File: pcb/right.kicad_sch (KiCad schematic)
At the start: 114 parts, among them J1 PJ-320A, SW1 -, SW10 O, SW11 I, SW12 U, SW13 Y, SW14 ', SW15 ;, SW16 L, SW17 K, SW18 J, SW19 H, SW2 0, SW20 Alt, SW21 Shift, SW22 /, SW23 ., SW24 ,, SW25 M, SW26 N, SW27 Ctrl, SW28 ], SW29 [, SW3 9, SW30 Down, SW31 Up, SW32 Fn, SW33 Space, SW34 Enter, SW4 8, SW5 7, SW6 6, SW8 \, SW9 P, SW90 MSK12C02 power, SW91 Reset, U1 nRF52840 Pro Micro

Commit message: Merge both halves into one KiCad project
pcb/keygen.kicad_pro holds a top sheet with left and right sub-sheets
(refs 1xx/2xx, sheet-local nets) and will carry one PCB with both halves
joined by snap-off tabs. The board stays non-reversible. The checker now
runs ERC on the whole project and splits the netlist per half.
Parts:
- removed BT1: LiPo 3.7V ~1000mAh, Connector_JST:JST_PH_S2B-PH-K_1x02_P2.00mm_Horizontal, symbol Device:Battery_Cell
- removed C1: 10uF, Capacitor_SMD:C_0805_2012Metric, symbol Device:C
- removed C2: 100nF, Capacitor_SMD:C_0805_2012Metric, symbol Device:C
- removed D1, D10, D11, D12, D13, D14, D15, D16, D17, D18, D19, D2, D20, D21, D22, D23, D24, D25, D26, D27, D28, D29, D3, D30, D31, D32, D33, D34, D4, D5, D6, D7, D8, D9: 1N4148, Diode_THT:D_DO-35_SOD27_P7.62mm_Horizontal, symbol Device:D
- removed ENC1: EC11, Rotary_Encoder:RotaryEncoder_Alps_EC11E-Switch_Vertical_H20mm, symbol Device:RotaryEncoder_Switch
- removed J1: PJ-320A, Keebio-Parts:TRRS-PJ-320A, symbol keygen:TRRS_PJ-320A
- removed LED1, LED10, LED11, LED12, LED13, LED14, LED15, LED16, LED17, LED18, LED19, LED2, LED20, LED21, LED22, LED23, LED24, LED25, LED26, LED27, LED28, LED29, LED3, LED30, LED31, LED32, LED33, LED34, LED35, LED36, LED37, LED38, LED39, LED4, LED5, LED6, LED7, LED8, LED9: SK6812MINI-E, LED_SMD:LED_SK6812MINI-E_3.2x2.8mm_P1.5mm_ReverseMount, symbol LED:SK6812MINI-E
- removed SW1: -, marbastlib-mx:SW_MX_HS_CPG151101S11_1.25u, symbol marbastlib-mx:MX_SW_HS_CPG151101S11
- removed SW10: O, marbastlib-mx:SW_MX_HS_CPG151101S11_1u, symbol marbastlib-mx:MX_SW_HS_CPG151101S11
- removed SW11: I, marbastlib-mx:SW_MX_HS_CPG151101S11_1u, symbol marbastlib-mx:MX_SW_HS_CPG151101S11
- removed SW12: U, marbastlib-mx:SW_MX_HS_CPG151101S11_1u, symbol marbastlib-mx:MX_SW_HS_CPG151101S11
- removed SW13: Y, marbastlib-mx:SW_MX_HS_CPG151101S11_1u, symbol marbastlib-mx:MX_SW_HS_CPG151101S11
- removed SW14: ', marbastlib-mx:SW_MX_HS_CPG151101S11_1.25u, symbol marbastlib-mx:MX_SW_HS_CPG151101S11
- removed SW15: ;, marbastlib-mx:SW_MX_HS_CPG151101S11_1u, symbol marbastlib-mx:MX_SW_HS_CPG151101S11
- removed SW16: L, marbastlib-mx:SW_MX_HS_CPG151101S11_1u, symbol marbastlib-mx:MX_SW_HS_CPG151101S11
- removed SW17: K, marbastlib-mx:SW_MX_HS_CPG151101S11_1u, symbol marbastlib-mx:MX_SW_HS_CPG151101S11
- removed SW18: J, marbastlib-mx:SW_MX_HS_CPG151101S11_1u, symbol marbastlib-mx:MX_SW_HS_CPG151101S11
- removed SW19: H, marbastlib-mx:SW_MX_HS_CPG151101S11_1u, symbol marbastlib-mx:MX_SW_HS_CPG151101S11
- removed SW2: 0, marbastlib-mx:SW_MX_HS_CPG151101S11_1u, symbol marbastlib-mx:MX_SW_HS_CPG151101S11
- removed SW20: Alt, marbastlib-mx:SW_MX_HS_CPG151101S11_1u, symbol marbastlib-mx:MX_SW_HS_CPG151101S11
- removed SW21: Shift, marbastlib-mx:SW_MX_HS_CPG151101S11_1.25u, symbol marbastlib-mx:MX_SW_HS_CPG151101S11
- removed SW22: /, marbastlib-mx:SW_MX_HS_CPG151101S11_1u, symbol marbastlib-mx:MX_SW_HS_CPG151101S11
- removed SW23: ., marbastlib-mx:SW_MX_HS_CPG151101S11_1u, symbol marbastlib-mx:MX_SW_HS_CPG151101S11
- removed SW24: ,, marbastlib-mx:SW_MX_HS_CPG151101S11_1u, symbol marbastlib-mx:MX_SW_HS_CPG151101S11
- removed SW25: M, marbastlib-mx:SW_MX_HS_CPG151101S11_1u, symbol marbastlib-mx:MX_SW_HS_CPG151101S11
- removed SW26: N, marbastlib-mx:SW_MX_HS_CPG151101S11_1u, symbol marbastlib-mx:MX_SW_HS_CPG151101S11
- removed SW27: Ctrl, marbastlib-mx:SW_MX_HS_CPG151101S11_1u, symbol marbastlib-mx:MX_SW_HS_CPG151101S11
- removed SW28: ], marbastlib-mx:SW_MX_HS_CPG151101S11_1u, symbol marbastlib-mx:MX_SW_HS_CPG151101S11
- removed SW29: [, marbastlib-mx:SW_MX_HS_CPG151101S11_1u, symbol marbastlib-mx:MX_SW_HS_CPG151101S11
- removed SW3: 9, marbastlib-mx:SW_MX_HS_CPG151101S11_1u, symbol marbastlib-mx:MX_SW_HS_CPG151101S11
- removed SW30: Down, marbastlib-mx:SW_MX_HS_CPG151101S11_1u, symbol marbastlib-mx:MX_SW_HS_CPG151101S11
- removed SW31: Up, marbastlib-mx:SW_MX_HS_CPG151101S11_1u, symbol marbastlib-mx:MX_SW_HS_CPG151101S11
- removed SW32: Fn, marbastlib-mx:SW_MX_HS_CPG151101S11_1.25u, symbol marbastlib-mx:MX_SW_HS_CPG151101S11
- removed SW33: Space, marbastlib-mx:SW_MX_HS_CPG151101S11_1.5u, symbol marbastlib-mx:MX_SW_HS_CPG151101S11
- removed SW34: Enter, marbastlib-mx:SW_MX_HS_CPG151101S11_1.5u, symbol marbastlib-mx:MX_SW_HS_CPG151101S11
- removed SW4: 8, marbastlib-mx:SW_MX_HS_CPG151101S11_1u, symbol marbastlib-mx:MX_SW_HS_CPG151101S11
- removed SW5: 7, marbastlib-mx:SW_MX_HS_CPG151101S11_1u, symbol marbastlib-mx:MX_SW_HS_CPG151101S11
- removed SW6: 6, marbastlib-mx:SW_MX_HS_CPG151101S11_1u, symbol marbastlib-mx:MX_SW_HS_CPG151101S11
- removed SW8: \, marbastlib-mx:SW_MX_HS_CPG151101S11_1.25u, symbol marbastlib-mx:MX_SW_HS_CPG151101S11
- removed SW9: P, marbastlib-mx:SW_MX_HS_CPG151101S11_1u, symbol marbastlib-mx:MX_SW_HS_CPG151101S11
- removed SW90: MSK12C02 power, marbastlib-various:SW_MSK12C02-HB, symbol Switch:SW_SPDT
- removed SW91: Reset, Button_Switch_THT:SW_PUSH_6mm_H5mm, symbol Switch:SW_Push
- removed U1: nRF52840 Pro Micro, marbastlib-xp-promicroish:nice_nano_H_USBup, symbol keygen:nice_nano_v2
- added BT201: LiPo 3.7V ~1000mAh, Connector_JST:JST_PH_S2B-PH-K_1x02_P2.00mm_Horizontal, symbol Device:Battery_Cell
- added C201: 10uF, Capacitor_SMD:C_0805_2012Metric, symbol Device:C
- added C202: 100nF, Capacitor_SMD:C_0805_2012Metric, symbol Device:C
- added D201, D202, D203, D204, D205, D206, D207, D208, D209, D210, D211, D212, D213, D214, D215, D216, D217, D218, D219, D220, D221, D222, D223, D224, D225, D226, D227, D228, D229, D230, D231, D232, D233, D234: 1N4148, Diode_THT:D_DO-35_SOD27_P7.62mm_Horizontal, symbol Device:D
- added ENC201: EC11, Rotary_Encoder:RotaryEncoder_Alps_EC11E-Switch_Vertical_H20mm, symbol Device:RotaryEncoder_Switch
- added J201: PJ-320A, Keebio-Parts:TRRS-PJ-320A, symbol keygen:TRRS_PJ-320A
- added LED201, LED202, LED203, LED204, LED205, LED206, LED207, LED208, LED209, LED210, LED211, LED212, LED213, LED214, LED215, LED216, LED217, LED218, LED219, LED220, LED221, LED222, LED223, LED224, LED225, LED226, LED227, LED228, LED229, LED230, LED231, LED232, LED233, LED234, LED235, LED236, LED237, LED238, LED239: SK6812MINI-E, LED_SMD:LED_SK6812MINI-E_3.2x2.8mm_P1.5mm_ReverseMount, symbol LED:SK6812MINI-E
- added SW201: -, marbastlib-mx:SW_MX_HS_CPG151101S11_1.25u, symbol marbastlib-mx:MX_SW_HS_CPG151101S11
- added SW202: 0, marbastlib-mx:SW_MX_HS_CPG151101S11_1u, symbol marbastlib-mx:MX_SW_HS_CPG151101S11
- added SW203: 9, marbastlib-mx:SW_MX_HS_CPG151101S11_1u, symbol marbastlib-mx:MX_SW_HS_CPG151101S11
- added SW204: 8, marbastlib-mx:SW_MX_HS_CPG151101S11_1u, symbol marbastlib-mx:MX_SW_HS_CPG151101S11
- added SW205: 7, marbastlib-mx:SW_MX_HS_CPG151101S11_1u, symbol marbastlib-mx:MX_SW_HS_CPG151101S11
- added SW206: 6, marbastlib-mx:SW_MX_HS_CPG151101S11_1u, symbol marbastlib-mx:MX_SW_HS_CPG151101S11
- added SW208: \, marbastlib-mx:SW_MX_HS_CPG151101S11_1.25u, symbol marbastlib-mx:MX_SW_HS_CPG151101S11
- added SW209: P, marbastlib-mx:SW_MX_HS_CPG151101S11_1u, symbol marbastlib-mx:MX_SW_HS_CPG151101S11
- added SW210: O, marbastlib-mx:SW_MX_HS_CPG151101S11_1u, symbol marbastlib-mx:MX_SW_HS_CPG151101S11
- added SW211: I, marbastlib-mx:SW_MX_HS_CPG151101S11_1u, symbol marbastlib-mx:MX_SW_HS_CPG151101S11
- added SW212: U, marbastlib-mx:SW_MX_HS_CPG151101S11_1u, symbol marbastlib-mx:MX_SW_HS_CPG151101S11
- added SW213: Y, marbastlib-mx:SW_MX_HS_CPG151101S11_1u, symbol marbastlib-mx:MX_SW_HS_CPG151101S11
- added SW214: ', marbastlib-mx:SW_MX_HS_CPG151101S11_1.25u, symbol marbastlib-mx:MX_SW_HS_CPG151101S11
- added SW215: ;, marbastlib-mx:SW_MX_HS_CPG151101S11_1u, symbol marbastlib-mx:MX_SW_HS_CPG151101S11
- added SW216: L, marbastlib-mx:SW_MX_HS_CPG151101S11_1u, symbol marbastlib-mx:MX_SW_HS_CPG151101S11
- added SW217: K, marbastlib-mx:SW_MX_HS_CPG151101S11_1u, symbol marbastlib-mx:MX_SW_HS_CPG151101S11
- added SW218: J, marbastlib-mx:SW_MX_HS_CPG151101S11_1u, symbol marbastlib-mx:MX_SW_HS_CPG151101S11
- added SW219: H, marbastlib-mx:SW_MX_HS_CPG151101S11_1u, symbol marbastlib-mx:MX_SW_HS_CPG151101S11
- added SW220: Alt, marbastlib-mx:SW_MX_HS_CPG151101S11_1u, symbol marbastlib-mx:MX_SW_HS_CPG151101S11
- added SW221: Shift, marbastlib-mx:SW_MX_HS_CPG151101S11_1.25u, symbol marbastlib-mx:MX_SW_HS_CPG151101S11
- added SW222: /, marbastlib-mx:SW_MX_HS_CPG151101S11_1u, symbol marbastlib-mx:MX_SW_HS_CPG151101S11
- added SW223: ., marbastlib-mx:SW_MX_HS_CPG151101S11_1u, symbol marbastlib-mx:MX_SW_HS_CPG151101S11
- added SW224: ,, marbastlib-mx:SW_MX_HS_CPG151101S11_1u, symbol marbastlib-mx:MX_SW_HS_CPG151101S11
- added SW225: M, marbastlib-mx:SW_MX_HS_CPG151101S11_1u, symbol marbastlib-mx:MX_SW_HS_CPG151101S11
- added SW226: N, marbastlib-mx:SW_MX_HS_CPG151101S11_1u, symbol marbastlib-mx:MX_SW_HS_CPG151101S11
- added SW227: Ctrl, marbastlib-mx:SW_MX_HS_CPG151101S11_1u, symbol marbastlib-mx:MX_SW_HS_CPG151101S11
- added SW228: ], marbastlib-mx:SW_MX_HS_CPG151101S11_1u, symbol marbastlib-mx:MX_SW_HS_CPG151101S11
- added SW229: [, marbastlib-mx:SW_MX_HS_CPG151101S11_1u, symbol marbastlib-mx:MX_SW_HS_CPG151101S11
- added SW230: Down, marbastlib-mx:SW_MX_HS_CPG151101S11_1u, symbol marbastlib-mx:MX_SW_HS_CPG151101S11
- added SW231: Up, marbastlib-mx:SW_MX_HS_CPG151101S11_1u, symbol marbastlib-mx:MX_SW_HS_CPG151101S11
- added SW232: Fn, marbastlib-mx:SW_MX_HS_CPG151101S11_1.25u, symbol marbastlib-mx:MX_SW_HS_CPG151101S11
- added SW233: Space, marbastlib-mx:SW_MX_HS_CPG151101S11_1.5u, symbol marbastlib-mx:MX_SW_HS_CPG151101S11
- added SW234: Enter, marbastlib-mx:SW_MX_HS_CPG151101S11_1.5u, symbol marbastlib-mx:MX_SW_HS_CPG151101S11
- added SW290: MSK12C02 power, marbastlib-various:SW_MSK12C02-HB, symbol Switch:SW_SPDT
- added SW291: Reset, Button_Switch_THT:SW_PUSH_6mm_H5mm, symbol Switch:SW_Push
- added U201: nRF52840 Pro Micro, marbastlib-xp-promicroish:nice_nano_H_USBup, symbol keygen:nice_nano_v2
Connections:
- net BAT_RAW: now also BT201.1 (+), SW290.1 (A)
- net COL0: now also SW201.1, SW208.1, SW214.1, SW221.1, SW228.1, U201.12 (P1.06)
- net COL1: now also SW202.1, SW209.1, SW215.1, SW222.1, SW229.1, U201.22 (P1.11)
- net COL2: now also SW203.1, SW210.1, SW216.1, SW223.1, SW230.1, U201.21 (P1.13)
- net COL3: now also SW204.1, SW211.1, SW217.1, SW224.1, SW231.1, U201.20 (P1.15)
- net COL4: now also SW205.1, SW212.1, SW218.1, SW225.1, SW232.1, U201.19 (P0.02)
- net COL5: now also SW206.1, SW213.1, SW219.1, SW226.1, SW233.1, U201.18 (P0.29)
- net COL6: now also ENC201.S1, SW220.1, SW227.1, SW234.1, U201.17 (P0.31)
- net ENC_A: now also ENC201.A, U201.6 (P0.20)
- net ENC_B: now also ENC201.B, U201.24 (P0.09)
- net GND: now also BT201.2 (-), C201.2, C202.2, ENC201.C, J201.1 (S), LED201.1 (VSS), LED202.1 (VSS), LED203.1 (VSS), LED204.1 (VSS), LED205.1 (VSS), LED206.1 (VSS), LED207.1 (VSS), LED208.1 (VSS), LED209.1 (VSS), LED210.1 (VSS), LED211.1 (VSS), LED212.1 (VSS), LED213.1 (VSS), LED214.1 (VSS), LED215.1 (VSS), LED216.1 (VSS), LED217.1 (VSS), LED218.1 (VSS), LED219.1 (VSS), LED220.1 (VSS), LED221.1 (VSS), LED222.1 (VSS), LED223.1 (VSS), LED224.1 (VSS), LED225.1 (VSS), LED226.1 (VSS), LED227.1 (VSS), LED228.1 (VSS), LED229.1 (VSS), LED230.1 (VSS), LED231.1 (VSS), LED232.1 (VSS), LED233.1 (VSS), LED234.1 (VSS), LED235.1 (VSS), LED236.1 (VSS), LED237.1 (VSS), LED238.1 (VSS), LED239.1 (VSS), SW291.2, U201.14 (GND), U201.3 (GND), U201.4 (GND)
- net K00: now also D201.2 (A), SW201.2
- net K01: now also D202.2 (A), SW202.2
- net K02: now also D203.2 (A), SW203.2
- net K03: now also D204.2 (A), SW204.2
- net K04: now also D205.2 (A), SW205.2
- net K05: now also D206.2 (A), SW206.2
- net K06: now also D207.2 (A), ENC201.S2
- net K10: now also D208.2 (A), SW208.2
- net K11: now also D209.2 (A), SW209.2
- net K12: now also D210.2 (A), SW210.2
- net K13: now also D211.2 (A), SW211.2
- net K14: now also D212.2 (A), SW212.2
- net K15: now also D213.2 (A), SW213.2
- net K20: now also D214.2 (A), SW214.2
- net K21: now also D215.2 (A), SW215.2
- net K22: now also D216.2 (A), SW216.2
- net K23: now also D217.2 (A), SW217.2
- net K24: now also D218.2 (A), SW218.2
- net K25: now also D219.2 (A), SW219.2
- net K26: now also D220.2 (A), SW220.2
- net K30: now also D221.2 (A), SW221.2
- net K31: now also D222.2 (A), SW222.2
- net K32: now also D223.2 (A), SW223.2
- net K33: now also D224.2 (A), SW224.2
- net K34: now also D225.2 (A), SW225.2
- net K35: now also D226.2 (A), SW226.2
- net K36: now also D227.2 (A), SW227.2
- net K40: now also D228.2 (A), SW228.2
- net K41: now also D229.2 (A), SW229.2
- net K42: now also D230.2 (A), SW230.2
- net K43: now also D231.2 (A), SW231.2
- net K44: now also D232.2 (A), SW232.2
- net K45: now also D233.2 (A), SW233.2
- net K46: now also D234.2 (A), SW234.2
- net LED_D1: now also LED201.4 (DOUT), LED202.2 (DIN)
- net LED_D10: now also LED210.4 (DOUT), LED211.2 (DIN)
- net LED_D11: now also LED211.4 (DOUT), LED212.2 (DIN)
- net LED_D12: now also LED212.4 (DOUT), LED213.2 (DIN)
- net LED_D13: now also LED213.4 (DOUT), LED214.2 (DIN)
- net LED_D14: now also LED214.4 (DOUT), LED215.2 (DIN)
- net LED_D15: now also LED215.4 (DOUT), LED216.2 (DIN)
- net LED_D16: now also LED216.4 (DOUT), LED217.2 (DIN)
- net LED_D17: now also LED217.4 (DOUT), LED218.2 (DIN)
- net LED_D18: now also LED218.4 (DOUT), LED219.2 (DIN)
- net LED_D19: now also LED219.4 (DOUT), LED220.2 (DIN)
- net LED_D2: now also LED202.4 (DOUT), LED203.2 (DIN)
- net LED_D20: now also LED220.4 (DOUT), LED221.2 (DIN)
- net LED_D21: now also LED221.4 (DOUT), LED222.2 (DIN)
- net LED_D22: now also LED222.4 (DOUT), LED223.2 (DIN)
- net LED_D23: now also LED223.4 (DOUT), LED224.2 (DIN)
- net LED_D24: now also LED224.4 (DOUT), LED225.2 (DIN)
- net LED_D25: now also LED225.4 (DOUT), LED226.2 (DIN)
- net LED_D26: now also LED226.4 (DOUT), LED227.2 (DIN)
- net LED_D27: now also LED227.4 (DOUT), LED228.2 (DIN)
- net LED_D28: now also LED228.4 (DOUT), LED229.2 (DIN)
- net LED_D29: now also LED229.4 (DOUT), LED230.2 (DIN)
- net LED_D3: now also LED203.4 (DOUT), LED204.2 (DIN)
- net LED_D30: now also LED230.4 (DOUT), LED231.2 (DIN)
- net LED_D31: now also LED231.4 (DOUT), LED232.2 (DIN)
- net LED_D32: now also LED232.4 (DOUT), LED233.2 (DIN)
- net LED_D33: now also LED233.4 (DOUT), LED234.2 (DIN)
- net LED_D34: now also LED234.4 (DOUT), LED235.2 (DIN)
- net LED_D35: now also LED235.4 (DOUT), LED236.2 (DIN)
- net LED_D36: now also LED236.4 (DOUT), LED237.2 (DIN)
- net LED_D37: now also LED237.4 (DOUT), LED238.2 (DIN)
- net LED_D38: now also LED238.4 (DOUT), LED239.2 (DIN)
- net LED_D4: now also LED204.4 (DOUT), LED205.2 (DIN)
- net LED_D5: now also LED205.4 (DOUT), LED206.2 (DIN)
- net LED_D6: now also LED206.4 (DOUT), LED207.2 (DIN)
- net LED_D7: now also LED207.4 (DOUT), LED208.2 (DIN)
- net LED_D8: now also LED208.4 (DOUT), LED209.2 (DIN)
- net LED_D9: now also LED209.4 (DOUT), LED210.2 (DIN)
- net LED_DIN: now also LED201.2 (DIN), U201.1 (P0.06)
- net ROW0: now also D201.1 (K), D202.1 (K), D203.1 (K), D204.1 (K), D205.1 (K), D206.1 (K), D207.1 (K), U201.7 (P0.22)
- net ROW1: now also D208.1 (K), D209.1 (K), D210.1 (K), D211.1 (K), D212.1 (K), D213.1 (K), U201.8 (P0.24)
- net ROW2: now also D214.1 (K), D215.1 (K), D216.1 (K), D217.1 (K), D218.1 (K), D219.1 (K), D220.1 (K), U201.9 (P1.00)
- net ROW3: now also D221.1 (K), D222.1 (K), D223.1 (K), D224.1 (K), D225.1 (K), D226.1 (K), D227.1 (K), U201.10 (P0.11)
- net ROW4: now also D228.1 (K), D229.1 (K), D230.1 (K), D231.1 (K), D232.1 (K), D233.1 (K), D234.1 (K), U201.11 (P1.04)
- net RST: now also SW291.1, U201.15 (RST)
- net UART_RX: now also J201.3 (R1), U201.5 (P0.17)
- net UART_TX: now also J201.2 (T), U201.2 (P0.08)
- net VBAT: now also SW290.2 (B), U201.13 (B+)
- net VCC: now also C201.1, C202.1, LED201.3 (VDD), LED202.3 (VDD), LED203.3 (VDD), LED204.3 (VDD), LED205.3 (VDD), LED206.3 (VDD), LED207.3 (VDD), LED208.3 (VDD), LED209.3 (VDD), LED210.3 (VDD), LED211.3 (VDD), LED212.3 (VDD), LED213.3 (VDD), LED214.3 (VDD), LED215.3 (VDD), LED216.3 (VDD), LED217.3 (VDD), LED218.3 (VDD), LED219.3 (VDD), LED220.3 (VDD), LED221.3 (VDD), LED222.3 (VDD), LED223.3 (VDD), LED224.3 (VDD), LED225.3 (VDD), LED226.3 (VDD), LED227.3 (VDD), LED228.3 (VDD), LED229.3 (VDD), LED230.3 (VDD), LED231.3 (VDD), LED232.3 (VDD), LED233.3 (VDD), LED234.3 (VDD), LED235.3 (VDD), LED236.3 (VDD), LED237.3 (VDD), LED238.3 (VDD), LED239.3 (VDD), U201.16 (VCC)
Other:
- note added: "Encoder S1/S2 (see ENC201)"
- note removed: "Encoder S1/S2 (see ENC1)"

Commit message: Mark switch bodies on the front silkscreen
pcb/lib/keygen.pretty holds marbastlib's MX hotswap footprints with a
14 mm switch outline on B.SilkS, which lands on the front because the
footprints are placed flipped. Keeping it in a project library (instead
of editing placed footprints) avoids library-mismatch warnings and keeps
'update footprints from library' safe.
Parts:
- SW201, SW208, SW214, SW221, SW232: footprint marbastlib-mx:SW_MX_HS_CPG151101S11_1.25u -> keygen:SW_MX_HS_CPG151101S11_1.25u
- SW202, SW203, SW204, SW205, SW206, SW209, SW210, SW211, SW212, SW213, SW215, SW216, SW217, SW218, SW219, SW220, SW222, SW223, SW224, SW225, SW226, SW227, SW228, SW229, SW230, SW231: footprint marbastlib-mx:SW_MX_HS_CPG151101S11_1u -> keygen:SW_MX_HS_CPG151101S11_1u
- SW233, SW234: footprint marbastlib-mx:SW_MX_HS_CPG151101S11_1.5u -> keygen:SW_MX_HS_CPG151101S11_1.5u

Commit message: Show switches, keycaps and parts in KiCad's 3D view
Project copies of the vendored footprints point their 3D models inside
the repo. The hotswap footprints add a kiswitch MX switch and a generated
keycap, turned over so they stand on the front of a back-mounted part.
The controller gets a simple generated block. The encoder moves to
marbastlib's EC11 footprint (origin at the shaft) because KiCad's
encoder model isn't in the 3D package. Renders in docs/.
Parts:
- ENC201: footprint Rotary_Encoder:RotaryEncoder_Alps_EC11E-Switch_Vertical_H20mm -> keygen:ROT_Alps_EC11E-Switch
- J201: footprint Keebio-Parts:TRRS-PJ-320A -> keygen:TRRS-PJ-320A
- SW290: footprint marbastlib-various:SW_MSK12C02-HB -> keygen:SW_MSK12C02-HB
- U201: footprint marbastlib-xp-promicroish:nice_nano_H_USBup -> keygen:nice_nano_H_USBup

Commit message: Route the PCB: DRC clean with schematic parity
Freerouting routes ~85% of signals with ground left to the pour; a grid
maze router (finish_route.py) completes the rest and ties stranded
ground pads to vias. Ground is poured on both layers per half with
stitching vias, islands removed and an antenna keep-out under each
controller. sync_pcb.py relinks footprints to the schematic; schematic
UUIDs are now deterministic so regenerating keeps those links, and the
generator no longer overwrites the project's design rules. Mounting
holes are in the schematic. Result: 0 unconnected, 0 errors, 0 parity
issues (28 silkscreen warnings remain).
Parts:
- added H201, H202, H203, H204, H205: M2, MountingHole:MountingHole_2.2mm_M2, symbol Mechanical:MountingHole
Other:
- note added: "MOUNTING HOLES (M2)"

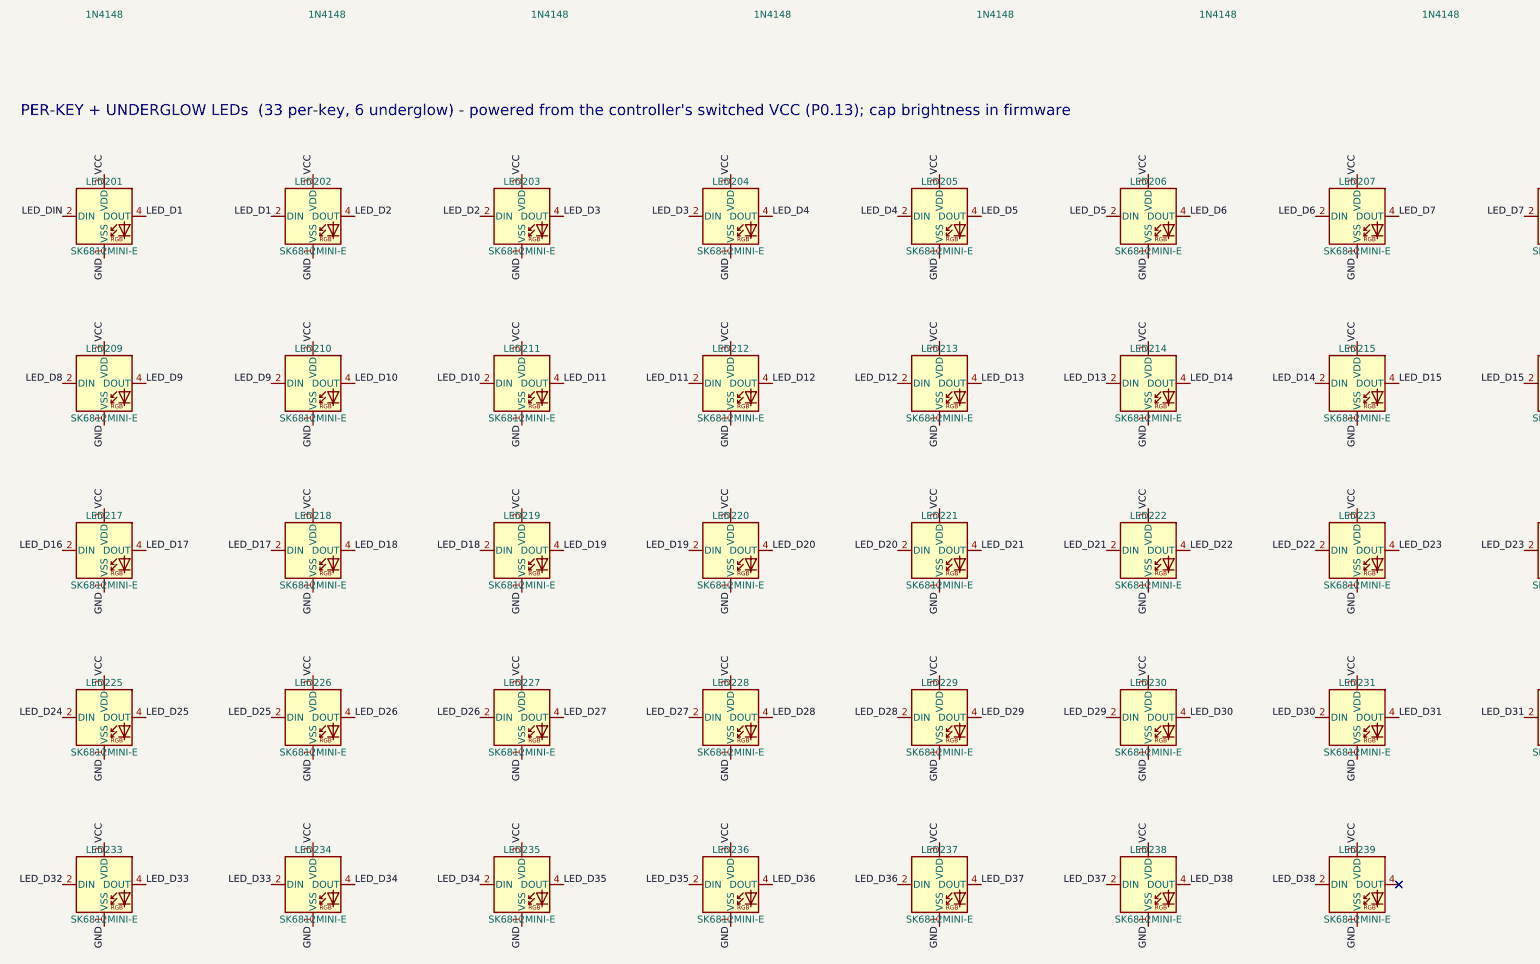
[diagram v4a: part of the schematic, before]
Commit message: Drop the underglow LEDs
The battery sits under the PCB, where it would hide the six underglow
LEDs per half and they would only drain it. The LED chain is now the 33
per-key LEDs on each half (LED x01-x33), all reverse-mounted on the back.

The schematic and placement generators no longer add them. On the routed
board the 12 footprints and their chain copper were removed, the VCC
links they carried were re-routed with finish_route.py, and DRC with
schematic parity is clean (0 errors, 0 unconnected). Gerbers, BOMs, the
schematic PDF, the plan and the shopping list are regenerated.

(Cherry-picked from 8c0cb53, made on the board before the tracks were
straightened; the board surgery, VCC re-route and outputs were redone
on the straightened board.)
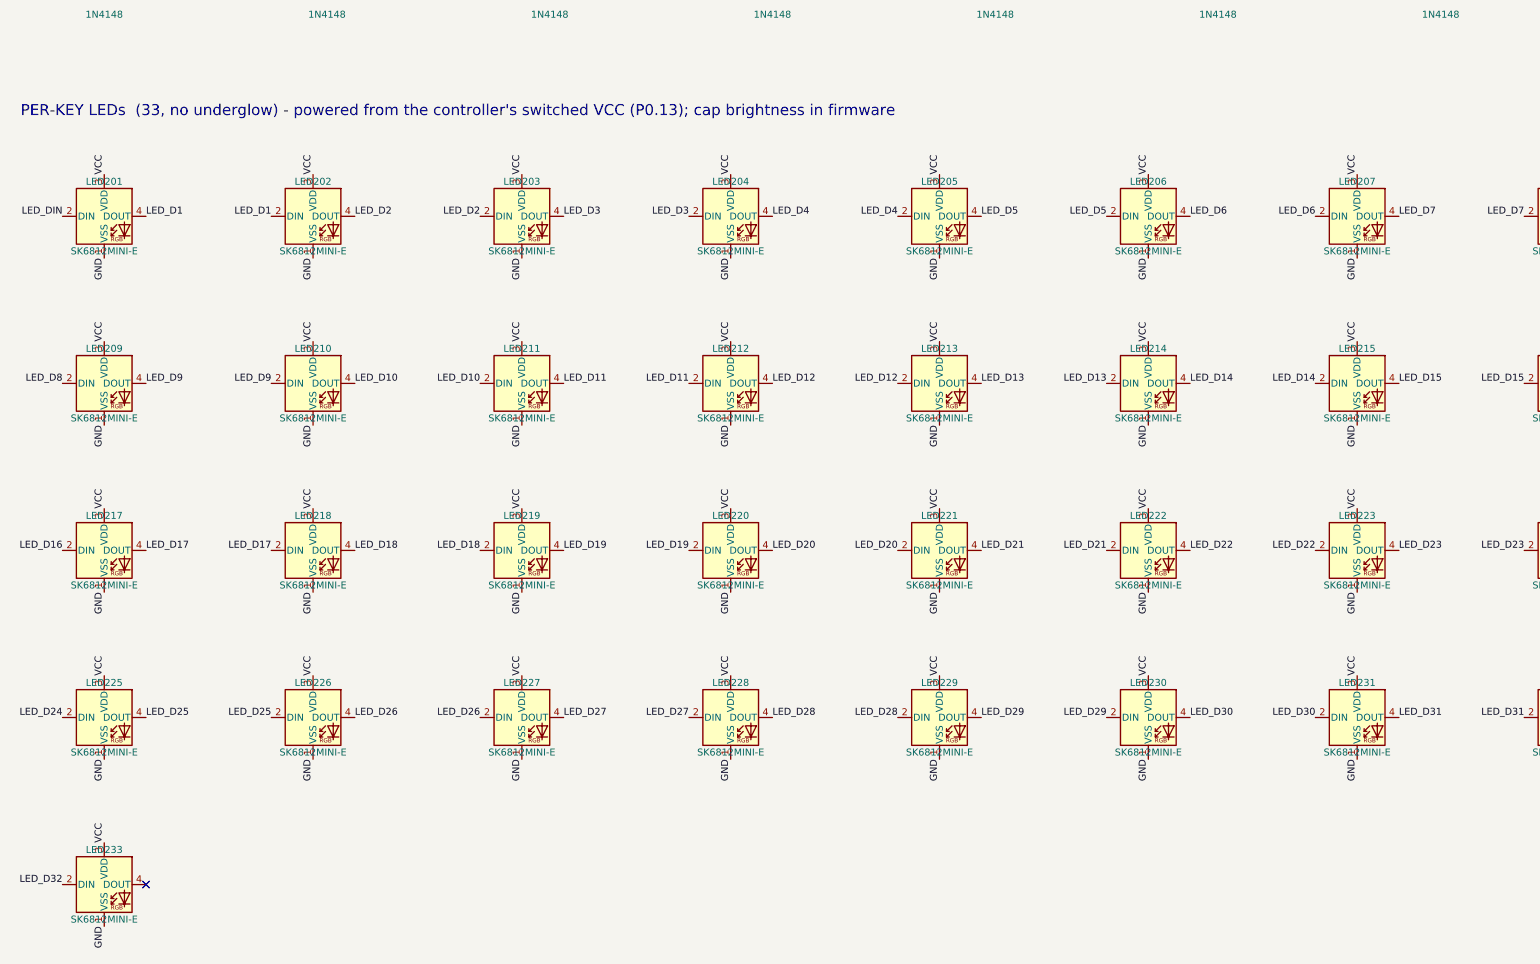
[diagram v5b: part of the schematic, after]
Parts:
- removed LED234, LED235, LED236, LED237, LED238, LED239: SK6812MINI-E, LED_SMD:LED_SK6812MINI-E_3.2x2.8mm_P1.5mm_ReverseMount, symbol LED:SK6812MINI-E
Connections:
- net LED_D33: no longer names the net of LED233.4 (DOUT)
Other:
- note added: "PER-KEY LEDs (33, no underglow) - powered from the controller's switched VCC (P0.13); cap brightness in firmware"
- note removed: "PER-KEY + UNDERGLOW LEDs (33 per-key, 6 underglow) - powered from the controller's switched VCC (P0.13); cap brightness in firmware"
